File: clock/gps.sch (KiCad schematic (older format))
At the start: 9 parts

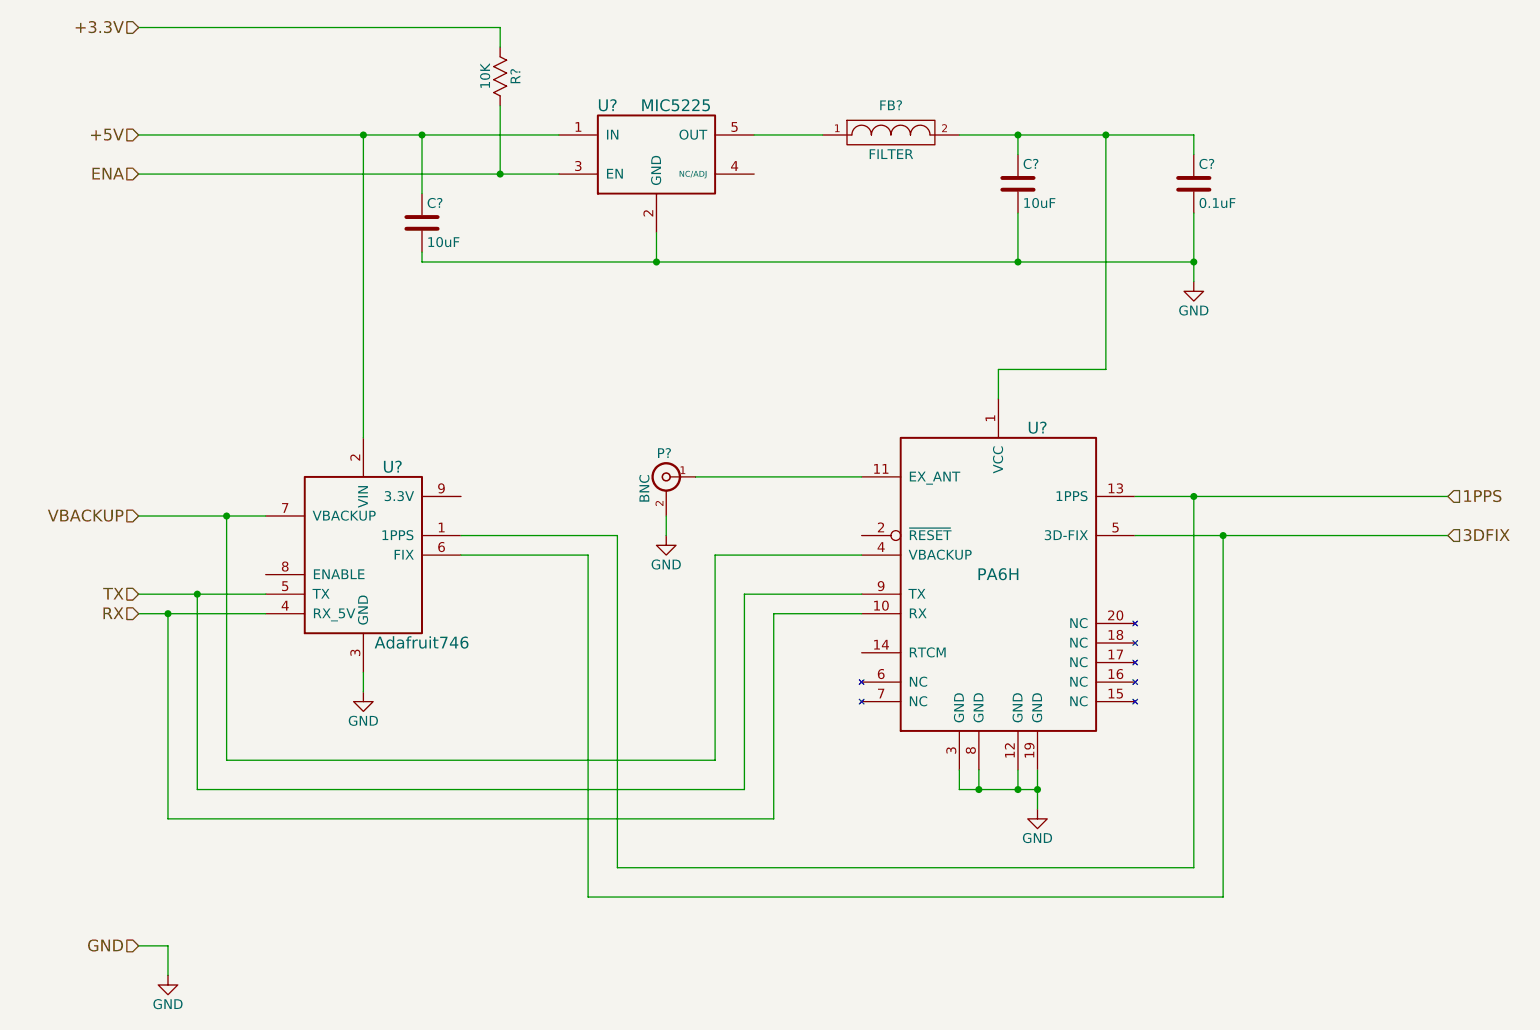
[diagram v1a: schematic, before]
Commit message: Update parts with parameter detail and BOM information.
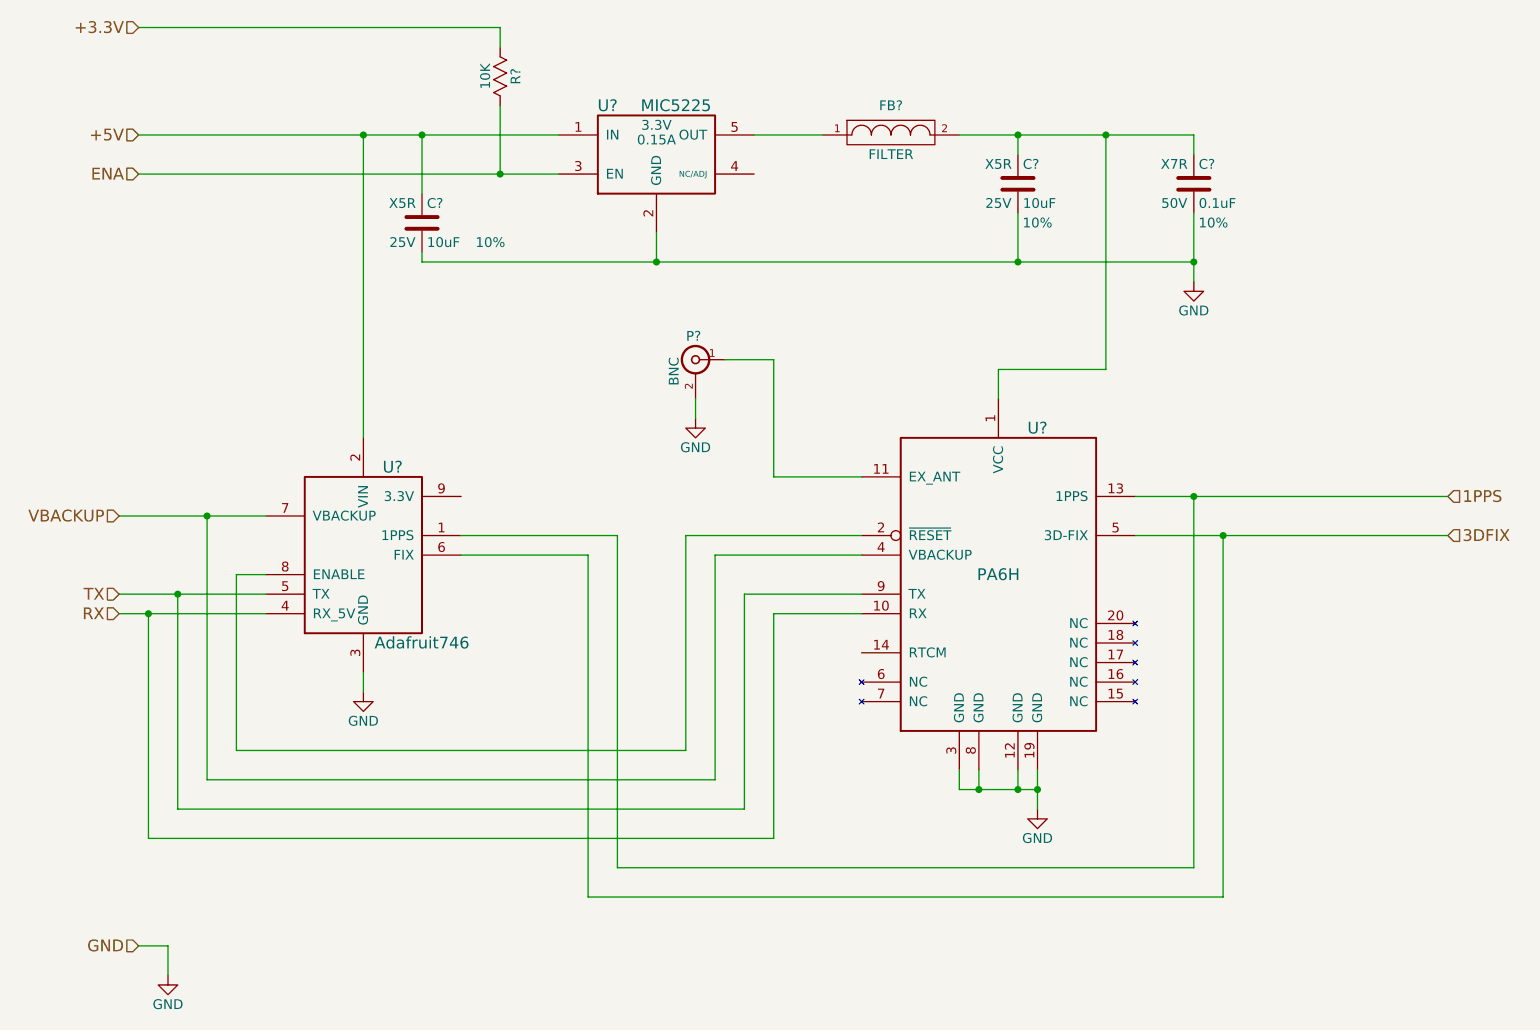
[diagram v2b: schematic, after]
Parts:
- removed C? (x2): 10uF, symbol C
- removed C?: 0.1uF, symbol C
- removed U?: Adafruit746, symbol Adafruit746
- removed U?: PA6H, symbol PA6H
- removed U?: MIC5225, symbol MIC5225
- added C? (x2): 10uF, Capacitors_SMD:C_1206_HandSoldering, symbol C
- added C?: 0.1uF, Capacitors_SMD:C_0805_HandSoldering, symbol C
- added U?: MIC5225, symbol MIC5225
- added U?: Adafruit746, symbol Adafruit746
- added U?: PA6H, symbol PA6H
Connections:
- net +5V: now also C?.1, U?.1 (IN), U?.2 (VIN)
- net 1PPS: now also U?.1 (1PPS), U?.13 (1PPS)
- net 3DFIX: now also U?.5 (3D-FIX), U?.6 (FIX)
- net ENA: now also U?.3 (EN)
- net GND: now also C?.2, C?.2, C?.2, U?.12 (GND), U?.19 (GND), U?.2 (GND), U?.3 (GND), U?.3 (GND), U?.8 (GND)
- net RX: now also U?.10 (RX), U?.4 (RX_5V)
- net TX: now also U?.5 (TX), U?.9 (TX)
- net VBACKUP: now also U?.4 (VBACKUP), U?.7 (VBACKUP)
- net at FB?.2: now also C?.1, C?.1, U?.1 (VCC)
- net at P?.1 (In): now also U?.11 (EX_ANT)
- net at FB?.1: now also U?.5 (OUT)
- new net: U?.2 (~RESET~), U?.8 (ENABLE)
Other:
- moved on the sheet: P?
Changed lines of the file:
@@
 $Descr A4 11693 8268
 encoding utf-8
-Sheet 4 5
+Sheet 3 5
 Title ""
 Date ""
@@
 $EndDescr
 $Comp
-L Adafruit746 U?
-U 1 1 56133D7D
-P 3750 4050
-F 0 "U?" H 3900 4500 60  0000 C CNN
-F 1 "Adafruit746" H 4050 3600 60  0000 C CNN
-F 2 "" H 3750 4050 60  0000 C CNN
-F 3 "" H 3750 4050 60  0000 C CNN
-	1    3750 4050
-	1    0    0    -1
-$EndComp
-$Comp
-L PA6H U?
-U 1 1 56133DD9
-P 7000 4150
-F 0 "U?" H 7200 4900 60  0000 C CNN
-F 1 "PA6H" H 7000 4150 60  0000 C CNN
-F 2 "" H 7500 4150 60  0000 C CNN
-F 3 "" H 7500 4150 60  0000 C CNN
-	1    7000 4150
-	1    0    0    -1
-$EndComp
-$Comp
-L MIC5225 U?
-U 1 1 56133E9A
-P 5250 2000
-AR Path="/56133E9A" Ref="U?"  Part="1"
-AR Path="/56133D72/56133E9A" Ref="U?"  Part="1"
-F 0 "U?" H 5000 2250 60  0000 C CNN
-F 1 "MIC5225" H 5350 2250 60  0000 C CNN
-F 2 "" H 5050 2000 60  0000 C CNN
-F 3 "" H 5050 2000 60  0000 C CNN
-	1    5250 2000
-	1    0    0    -1
-$EndComp
-$Comp
 L FILTER FB?
 U 1 1 561A31C6
@@
 $EndComp
 $Comp
-L C C?
-U 1 1 561A3203
-P 4050 2350
-F 0 "C?" H 4075 2450 50  0000 L CNN
-F 1 "10uF" H 4075 2250 50  0000 L CNN
-F 2 "" H 4088 2200 30  0000 C CNN
-F 3 "" H 4050 2350 60  0000 C CNN
-	1    4050 2350
-	1    0    0    -1
-$EndComp
-$Comp
-L C C?
-U 1 1 561A3273
-P 8000 2150
-F 0 "C?" H 8025 2250 50  0000 L CNN
-F 1 "0.1uF" H 8025 2050 50  0000 L CNN
-F 2 "" H 8038 2000 30  0000 C CNN
-F 3 "" H 8000 2150 60  0000 C CNN
-	1    8000 2150
-	1    0    0    -1
-$EndComp
-$Comp
-L C C?
-U 1 1 561A32D8
-P 7100 2150
-F 0 "C?" H 7125 2250 50  0000 L CNN
-F 1 "10uF" H 7125 2050 50  0000 L CNN
-F 2 "" H 7138 2000 30  0000 C CNN
-F 3 "" H 7100 2150 60  0000 C CNN
-	1    7100 2150
-	1    0    0    -1
-$EndComp
-$Comp
 L BNC P?
 U 1 1 561A3335
-P 5300 3650
-F 0 "P?" H 5310 3770 50  0000 C CNN
-F 1 "BNC" V 5410 3590 50  0000 C CNN
-F 2 "" H 5300 3650 60  0000 C CNN
-F 3 "" H 5300 3650 60  0000 C CNN
-	1    5300 3650
+P 5450 3050
+F 0 "P?" H 5460 3170 50  0000 C CNN
+F 1 "BNC" V 5560 2990 50  0000 C CNN
+F 2 "" H 5450 3050 60  0000 C CNN
+F 3 "" H 5450 3050 60  0000 C CNN
+	1    5450 3050
 	-1   0    0    -1
 $EndComp
@@
 $EndComp
 Wire Wire Line
-	7200 5150 7200 5350
-Wire Wire Line
-	6800 5250 7200 5250
+	7200 5150 7200 5250
+Wire Wire Line
+	7200 5250 7200 5350
+Wire Wire Line
+	6800 5250 6900 5250
+Wire Wire Line
+	6900 5250 7100 5250
+Wire Wire Line
+	7100 5250 7200 5250
 Wire Wire Line
 	6800 5250 6800 5150
@@
 	5750 1900 6100 1900
 Wire Wire Line
-	6800 1900 8000 1900
+	6800 1900 7100 1900
+Wire Wire Line
+	7100 1900 7550 1900
+Wire Wire Line
+	7550 1900 8000 1900
 Wire Wire Line
 	7100 2000 7100 1900
@@
 $EndComp
 Wire Wire Line
-	2600 1900 4750 1900
+	2600 1900 3750 1900
+Wire Wire Line
+	3750 1900 4050 1900
+Wire Wire Line
+	4050 1900 4750 1900
 Wire Wire Line
 	4050 1900 4050 2200
@@
 	4050 2500 4050 2550
 Wire Wire Line
-	4050 2550 8000 2550
+	4050 2550 5250 2550
+Wire Wire Line
+	5250 2550 7100 2550
+Wire Wire Line
+	7100 2550 8000 2550
 Wire Wire Line
 	5250 2550 5250 2400
@@
 	4450 1750 4450 2100
 Wire Wire Line
-	2600 2100 4750 2100
+	2600 2100 4450 2100
+Wire Wire Line
+	4450 2100 4750 2100
 Wire Wire Line
 	4450 1450 4450 1350
@@
 Text HLabel 2600 1350 0    60   Input ~ 0
 +3.3V
-Text HLabel 2600 4250 0    60   Input ~ 0
+Text HLabel 2500 4250 0    60   Input ~ 0
 TX
-Text HLabel 2600 4350 0    60   Input ~ 0
+Text HLabel 2500 4350 0    60   Input ~ 0
 RX
 Wire Wire Line
-	5450 3650 6300 3650
+	5600 3050 5850 3050
+Wire Wire Line
+	5850 3050 5850 3650
+Wire Wire Line
+	5850 3650 6300 3650
 $Comp
 L GND #PWR?
 U 1 1 56236310
-P 5300 3950
-F 0 "#PWR?" H 5300 3700 50  0001 C CNN
-F 1 "GND" H 5300 3800 50  0000 C CNN
-F 2 "" H 5300 3950 60  0000 C CNN
-F 3 "" H 5300 3950 60  0000 C CNN
-	1    5300 3950
-	1    0    0    -1
-$EndComp
-Wire Wire Line
-	5300 3950 5300 3850
-Wire Wire Line
-	2600 4250 3250 4250
-Wire Wire Line
-	2600 4350 3250 4350
-Wire Wire Line
-	2600 3850 3250 3850
+P 5450 3350
+F 0 "#PWR?" H 5450 3100 50  0001 C CNN
+F 1 "GND" H 5450 3200 50  0000 C CNN
+F 2 "" H 5450 3350 60  0000 C CNN
+F 3 "" H 5450 3350 60  0000 C CNN
+	1    5450 3350
+	1    0    0    -1
+$EndComp
+Wire Wire Line
+	5450 3350 5450 3250
+Wire Wire Line
+	2500 4250 2800 4250
+Wire Wire Line
+	2800 4250 3250 4250
+Wire Wire Line
+	2500 4350 2650 4350
+Wire Wire Line
+	2650 4350 3250 4350
+Wire Wire Line
+	2500 3850 2950 3850
+Wire Wire Line
+	2950 3850 3250 3850
 $Comp
 L GND #PWR?
@@
 3DFIX
 Wire Wire Line
-	7700 3750 9300 3750
-Wire Wire Line
-	7700 3950 9300 3950
+	7700 3750 8000 3750
+Wire Wire Line
+	8000 3750 9300 3750
+Wire Wire Line
+	7700 3950 8150 3950
+Wire Wire Line
+	8150 3950 9300 3950
 Wire Wire Line
 	6300 4050 5550 4050
 Wire Wire Line
-	5550 4050 5550 5100
-Wire Wire Line
-	5550 5100 3050 5100
-Wire Wire Line
-	3050 5100 3050 3850
-Connection ~ 3050 3850
-Wire Wire Line
-	2900 4250 2900 5250
-Wire Wire Line
-	2900 5250 5700 5250
-Wire Wire Line
-	5700 5250 5700 4250
+	5550 4050 5550 5200
+Wire Wire Line
+	5550 5200 2950 5200
+Wire Wire Line
+	2950 5200 2950 3850
+Connection ~ 2950 3850
+Wire Wire Line
+	2800 4250 2800 5350
+Wire Wire Line
+	2800 5350 5700 5350
+Wire Wire Line
+	5700 5350 5700 4250
 Wire Wire Line
 	5700 4250 6300 4250
-Connection ~ 2900 4250
+Connection ~ 2800 4250
 Wire Wire Line
 	6300 4350 5850 4350
 Wire Wire Line
-	5850 4350 5850 5400
-Wire Wire Line
-	5850 5400 2750 5400
-Wire Wire Line
-	2750 5400 2750 4350
-Connection ~ 2750 4350
-Text HLabel 2600 3850 0    60   Input ~ 0
+	5850 4350 5850 5500
+Wire Wire Line
+	5850 5500 2650 5500
+Wire Wire Line
+	2650 5500 2650 4350
+Connection ~ 2650 4350
+Text HLabel 2500 3850 0    60   Input ~ 0
 VBACKUP
 Wire Wire Line
@@
 Connection ~ 7550 1900
 Wire Wire Line
-	8000 2300 8000 2650
+	8000 2300 8000 2550
+Wire Wire Line
+	8000 2550 8000 2650
 Connection ~ 8000 2550
 Wire Wire Line
@@
 Wire Wire Line
 	2750 6050 2600 6050
+$Comp
+L C C?
+U 1 1 5631FA60
+P 7100 2150
+F 0 "C?" H 7125 2250 50  0000 L CNN
+F 1 "10uF" H 7125 2050 50  0000 L CNN
+F 2 "Capacitors_SMD:C_1206_HandSoldering" H 7138 2000 30  0001 C CNN
+F 3 "" H 7100 2150 60  0000 C CNN
+F 4 "25V" H 7000 2050 50  0000 C CNN "Voltage"
+F 5 "10%" H 7200 1950 50  0000 C CNN "Tolerance"
+F 6 "X5R" H 7000 2250 50  0000 C CNN "Dielectric"
+F 7 "TDK" H 7100 2150 50  0001 C CNN "Manufacturer"
+F 8 "C3216X5R1E106K160AB" H 7100 2150 60  0001 C CNN "PartNum"
+	1    7100 2150
+	1    0    0    -1
+$EndComp
+$Comp
+L C C?
+U 1 1 5631FA6C
+P 8000 2150
+F 0 "C?" H 8025 2250 50  0000 L CNN
+F 1 "0.1uF" H 8025 2050 50  0000 L CNN
+F 2 "Capacitors_SMD:C_0805_HandSoldering" H 8038 2000 30  0001 C CNN
+F 3 "" H 8000 2150 60  0000 C CNN
+F 4 "50V" H 7900 2050 50  0000 C CNN "Voltage"
+F 5 "10%" H 8100 1950 50  0000 C CNN "Tolerance"
+F 6 "X7R" H 7900 2250 50  0000 C CNN "Dielectric"
+F 7 "Kemet" H 8000 2150 50  0001 C CNN "Manufacturer"
+F 8 "C0805C104K5RACTU" H 8000 2150 50  0001 C CNN "PartNum"
+	1    8000 2150
+	1    0    0    -1
+$EndComp
+$Comp
+L C C?
+U 1 1 5631FD2B
+P 4050 2350
+F 0 "C?" H 4075 2450 50  0000 L CNN
+F 1 "10uF" H 4075 2250 50  0000 L CNN
+F 2 "Capacitors_SMD:C_1206_HandSoldering" H 4088 2200 30  0001 C CNN
+F 3 "" H 4050 2350 60  0000 C CNN
+F 4 "25V" H 3950 2250 50  0000 C CNN "Voltage"
+F 5 "10%" H 4400 2250 50  0000 C CNN "Tolerance"
+F 6 "X5R" H 3950 2450 50  0000 C CNN "Dielectric"
+F 7 "TDK" H 4050 2350 50  0001 C CNN "Manufacturer"
+F 8 "C3216X5R1E106K160AB" H 4050 2350 60  0001 C CNN "PartNum"
+	1    4050 2350
+	1    0    0    -1
+$EndComp
+$Comp
+L MIC5225 U?
+U 1 1 563293EE
+P 5250 2000
+F 0 "U?" H 5000 2250 60  0000 C CNN
+F 1 "MIC5225" H 5350 2250 60  0000 C CNN
+F 2 "" H 5050 2000 60  0000 C CNN
+F 3 "" H 5050 2000 60  0000 C CNN
+F 4 "3.3V" H 5250 2150 50  0000 C CNN "Voltage"
+F 5 "0.15A" H 5250 2075 50  0000 C CNN "Current"
+F 6 "Micrel" H 5250 2425 50  0001 C CNN "Manufacturer"
+F 7 "MIC5225-3.3YM5-TR" H 5250 2350 50  0001 C CNN "PartNum"
+	1    5250 2000
+	1    0    0    -1
+$EndComp
+$Comp
+L Adafruit746 U?
+U 1 1 563295A6
+P 3750 4050
+F 0 "U?" H 3900 4500 60  0000 C CNN
+F 1 "Adafruit746" H 4050 3600 60  0000 C CNN
+F 2 "" H 3750 4050 60  0000 C CNN
+F 3 "" H 3900 4500 60  0000 C CNN
+F 4 "Adafruit" H 3950 3525 50  0001 C CNN "Manufacturer"
+F 5 "Adafruit746" H 4025 3450 50  0001 C CNN "PartNum"
+	1    3750 4050
+	1    0    0    -1
+$EndComp
+$Comp
+L PA6H U?
+U 1 1 56329634
+P 7000 4150
+F 0 "U?" H 7200 4900 60  0000 C CNN
+F 1 "PA6H" H 7000 4150 60  0000 C CNN
+F 2 "" H 7500 4150 60  0000 C CNN
+F 3 "" H 7500 4150 60  0000 C CNN
+F 4 "GlobalTop Technology" H 7000 4475 50  0001 C CNN "Manufacturer"
+F 5 "PA6H" H 7000 4075 50  0001 C CNN "PartNum"
+	1    7000 4150
+	1    0    0    -1
+$EndComp
+Wire Wire Line
+	6300 3950 5400 3950
+Wire Wire Line
+	5400 3950 5400 5050
+Wire Wire Line
+	5400 5050 3100 5050
+Wire Wire Line
+	3100 5050 3100 4150
+Wire Wire Line
+	3100 4150 3250 4150
 $EndSCHEMATC

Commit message: Add parameter for RF connector. Start adding display connections.
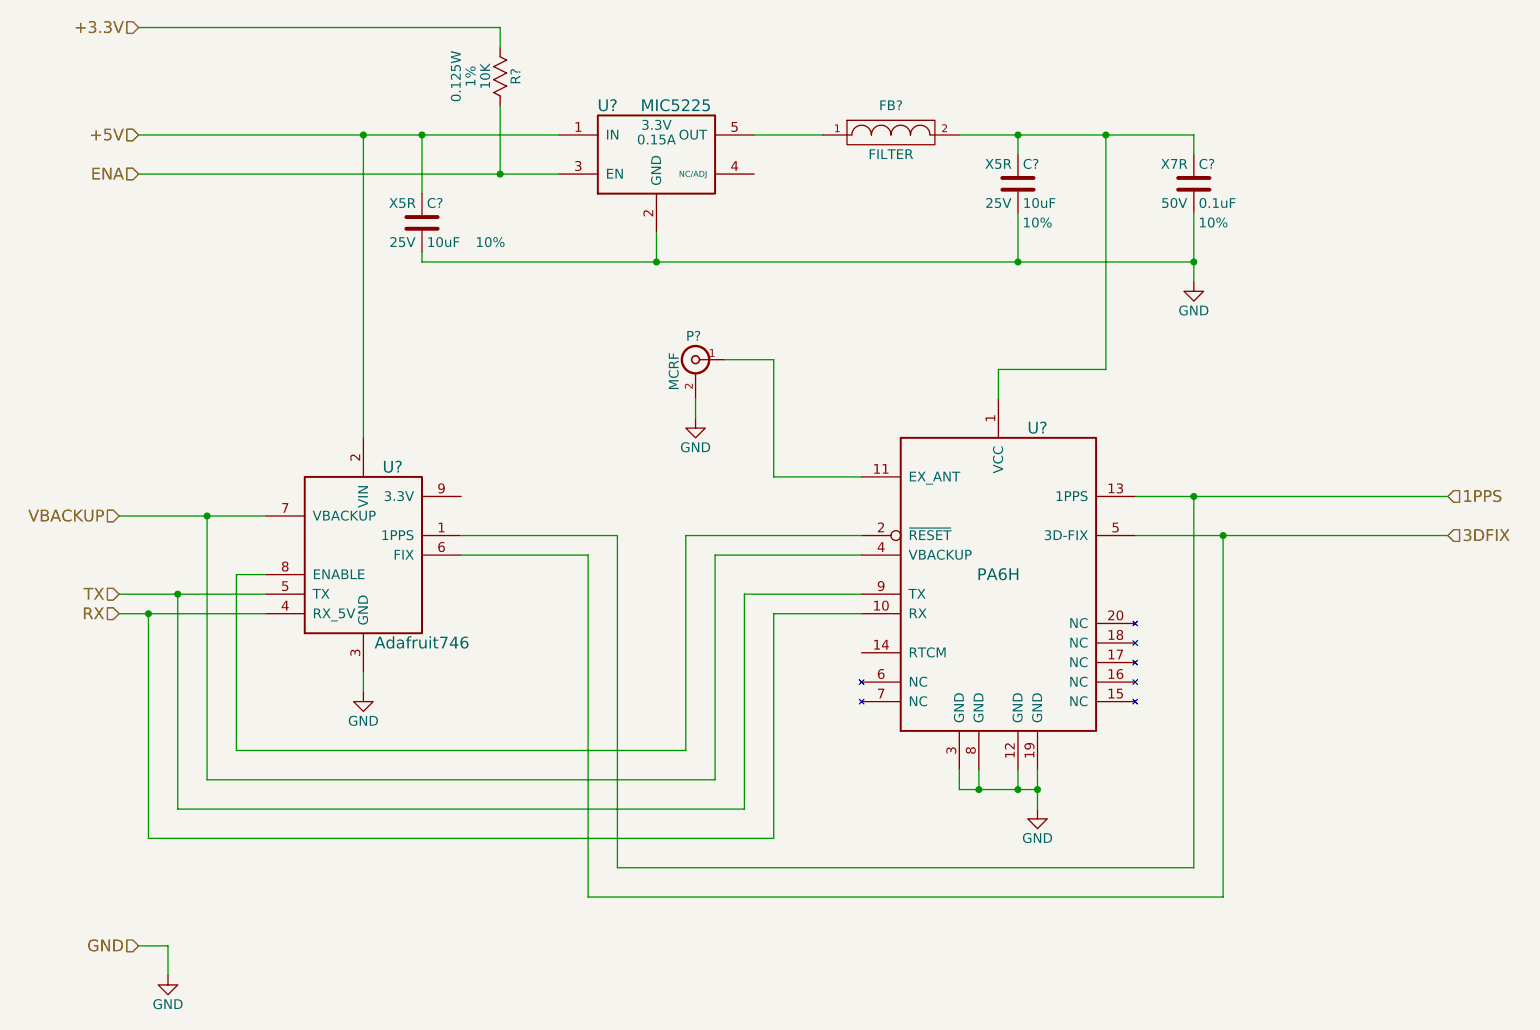
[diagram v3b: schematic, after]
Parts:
- removed R?: 10K, symbol R_local
- added R?: 10K, Resistors_SMD:R_0805_HandSoldering, symbol R_local
- P?: value BNC -> MCRF; Manufacturer (none) -> Molex; PartNum (none) -> 073412-0110
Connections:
- net +3.3V: now also R?.1
- net ENA: now also R?.2
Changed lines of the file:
@@
 P 5450 3050
 F 0 "P?" H 5460 3170 50  0000 C CNN
-F 1 "BNC" V 5560 2990 50  0000 C CNN
+F 1 "MCRF" V 5560 2990 50  0000 C CNN
 F 2 "" H 5450 3050 60  0000 C CNN
 F 3 "" H 5450 3050 60  0000 C CNN
+F 4 "Molex" H 5450 3050 50  0001 C CNN "Manufacturer"
+F 5 "073412-0110" H 5450 3050 50  0001 C CNN "PartNum"
 	1    5450 3050
 	-1   0    0    -1
@@
 $EndComp
 Wire Wire Line
-	7200 5150 7200 5250
-Wire Wire Line
-	7200 5250 7200 5350
-Wire Wire Line
-	6800 5250 6900 5250
-Wire Wire Line
-	6900 5250 7100 5250
-Wire Wire Line
-	7100 5250 7200 5250
+	7200 5150 7200 5350
+Wire Wire Line
+	6800 5250 7200 5250
 Wire Wire Line
 	6800 5250 6800 5150
@@
 	5750 1900 6100 1900
 Wire Wire Line
-	6800 1900 7100 1900
-Wire Wire Line
-	7100 1900 7550 1900
-Wire Wire Line
-	7550 1900 8000 1900
+	6800 1900 8000 1900
 Wire Wire Line
 	7100 2000 7100 1900
@@
 $EndComp
 Wire Wire Line
-	2600 1900 3750 1900
-Wire Wire Line
-	3750 1900 4050 1900
-Wire Wire Line
-	4050 1900 4750 1900
+	2600 1900 4750 1900
 Wire Wire Line
 	4050 1900 4050 2200
@@
 	4050 2500 4050 2550
 Wire Wire Line
-	4050 2550 5250 2550
-Wire Wire Line
-	5250 2550 7100 2550
-Wire Wire Line
-	7100 2550 8000 2550
+	4050 2550 8000 2550
 Wire Wire Line
 	5250 2550 5250 2400
 Connection ~ 5250 2550
 Connection ~ 7100 2550
-$Comp
-L R_local R?
-U 1 1 56235F17
-P 4450 1600
-F 0 "R?" V 4530 1600 50  0000 C CNN
-F 1 "10K" V 4375 1600 50  0000 C CNN
-F 2 "" V 4380 1600 30  0000 C CNN
-F 3 "" H 4450 1600 30  0000 C CNN
-	1    4450 1600
-	1    0    0    -1
-$EndComp
 Wire Wire Line
 	4450 1750 4450 2100
 Wire Wire Line
-	2600 2100 4450 2100
-Wire Wire Line
-	4450 2100 4750 2100
+	2600 2100 4750 2100
 Wire Wire Line
 	4450 1450 4450 1350
@@
 	5450 3350 5450 3250
 Wire Wire Line
-	2500 4250 2800 4250
-Wire Wire Line
-	2800 4250 3250 4250
-Wire Wire Line
-	2500 4350 2650 4350
-Wire Wire Line
-	2650 4350 3250 4350
-Wire Wire Line
-	2500 3850 2950 3850
-Wire Wire Line
-	2950 3850 3250 3850
+	2500 4250 3250 4250
+Wire Wire Line
+	2500 4350 3250 4350
+Wire Wire Line
+	2500 3850 3250 3850
 $Comp
 L GND #PWR?
@@
 3DFIX
 Wire Wire Line
-	7700 3750 8000 3750
-Wire Wire Line
-	8000 3750 9300 3750
-Wire Wire Line
-	7700 3950 8150 3950
-Wire Wire Line
-	8150 3950 9300 3950
+	7700 3750 9300 3750
+Wire Wire Line
+	7700 3950 9300 3950
 Wire Wire Line
 	6300 4050 5550 4050
@@
 Connection ~ 7550 1900
 Wire Wire Line
-	8000 2300 8000 2550
-Wire Wire Line
-	8000 2550 8000 2650
+	8000 2300 8000 2650
 Connection ~ 8000 2550
 Wire Wire Line
@@
 Wire Wire Line
 	3100 4150 3250 4150
+$Comp
+L R_local R?
+U 1 1 5632AC0C
+P 4450 1600
+F 0 "R?" V 4530 1600 50  0000 C CNN
+F 1 "10K" V 4375 1600 50  0000 C CNN
+F 2 "Resistors_SMD:R_0805_HandSoldering" V 4380 1600 30  0001 C CNN
+F 3 "" V 4530 1600 30  0000 C CNN
+F 4 "1%" V 4300 1600 50  0000 C CNN "Tolerance"
+F 5 "0.125W" V 4225 1600 50  0000 C CNN "Power"
+F 6 "Vishay Dale" V 4450 1600 50  0001 C CNN "Manufacturer"
+F 7 "CRCW080510K0FKEA" V 4600 1600 50  0001 C CNN "PartNum"
+	1    4450 1600
+	1    0    0    -1
+$EndComp
 $EndSCHEMATC
